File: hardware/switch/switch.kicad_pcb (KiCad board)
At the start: 2 copper layers, 70.5 x 70.5 mm, 27 parts, among them J1 Conn_01x07, J2 Conn_01x03, J3 Conn_01x05, J4 Conn_01x04, K1 G6SU-2, K2 G6SU-2, K3 G6SU-2, K4 G6SU-2, SW1 D2F-01, SW2 D2F-01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

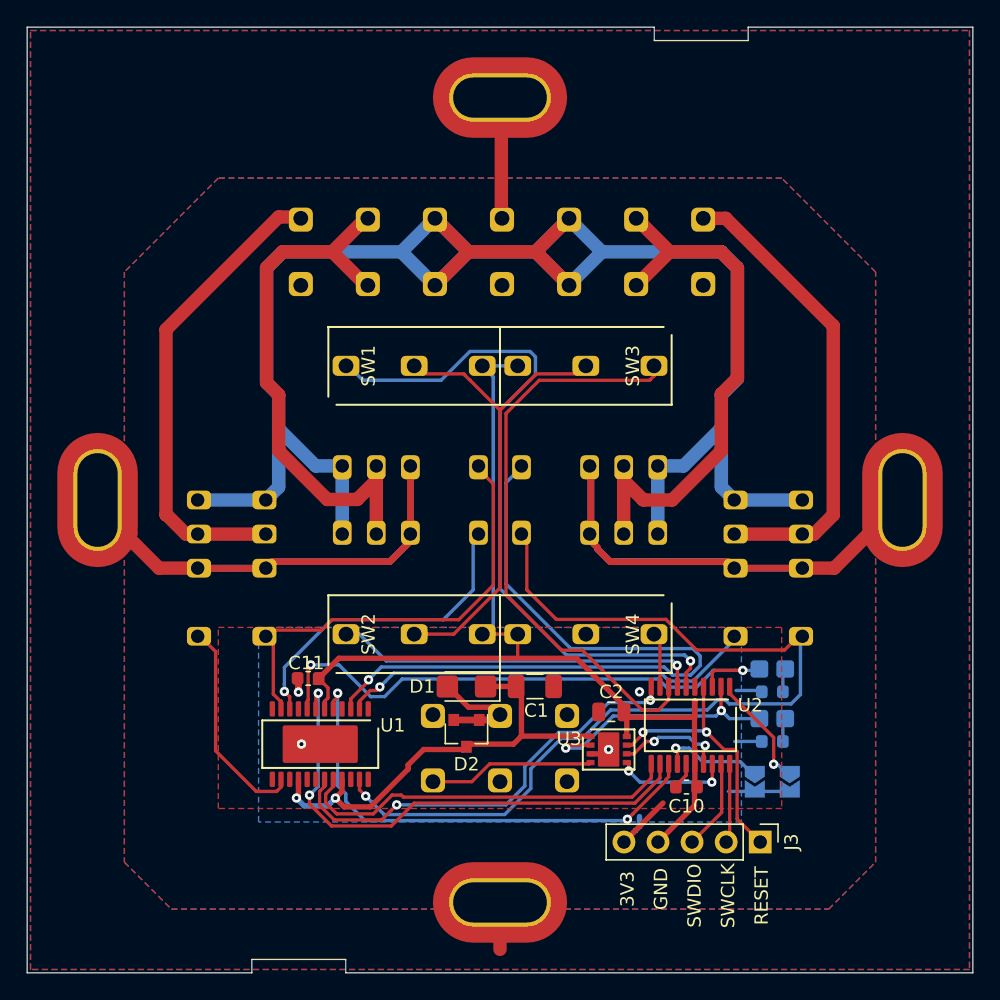
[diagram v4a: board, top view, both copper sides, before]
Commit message: Add indicator LEDs to switch
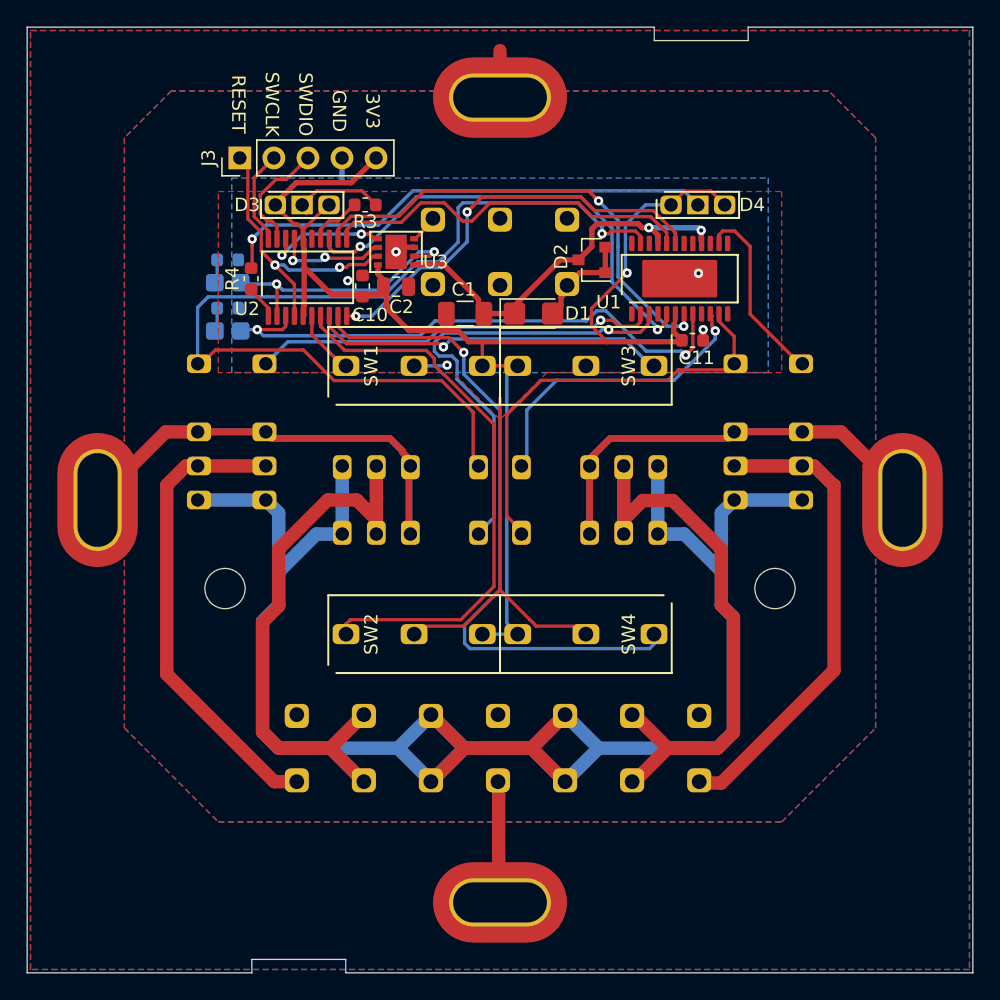
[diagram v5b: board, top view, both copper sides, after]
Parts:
- removed JP1, JP2: SolderJumper_2_Open, RoomControl:Jumper2
- added D5: LED, LED_SMD:LED_0805_2012Metric_Castellated, B.Cu at (79.7, 83.8)
- added D6: LED, LED_SMD:LED_0805_2012Metric_Castellated, B.Cu at (79.7, 87.4)
- added R3: 60R, Resistor_SMD:R_0603_1608Metric, F.Cu at (90.0, 78.0)
- added R4: 60R, Resistor_SMD:R_0603_1608Metric, F.Cu at (81.5, 83.5)
- D3, D4: value LED -> Conn_01x03; footprint LED_SMD:LED_0805_2012Metric_Castellated -> RoomControl:DiodeHoles3; moved to F.Cu
- moved J3 64.1 mm to (80.6, 74.5), turned to 90 degrees
- moved R1 54.2 mm to (79.7, 82.1), turned to 0 degrees
- moved D3 51.9 mm to (85.2, 78.0), turned to 0 degrees
- moved R2 49.7 mm to (79.7, 85.7), turned to 0 degrees
- moved J1 47.4 mm to (114.8, 118.5), turned to 90 degrees
- moved C10 44.5 mm to (89.8, 84.0), turned to 90 degrees
- moved U2 43.9 mm to (85.7, 83.4), turned to 90 degrees
- moved U1 43.8 mm to (113.4, 83.5), turned to 90 degrees
- moved U3 40.3 mm to (92.2, 81.5), turned to 180 degrees
- moved J2 38.3 mm to (105.0, 81.5), turned to 90 degrees
- moved C11 38.2 mm to (114.3, 88.1), turned to 0 degrees
- moved D2 36.5 mm to (106.8, 82.1), turned to 180 degrees
- moved C2 35.5 mm to (92.2, 84.1), turned to 0 degrees
- moved D4 35.0 mm to (114.8, 78.0), turned to 0 degrees
- moved C1 28.3 mm to (97.4, 86.1), turned to 180 degrees
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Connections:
- D3 pad 1: Net-(D3-Pad1) -> +3V3
- D3 pad 2: LIN_EN -> Net-(D3-Pad2)
- D4 pad 1: Net-(D4-Pad1) -> +3V3
- D4 pad 2: HB_EN -> Net-(D4-Pad2)
- J1 pad 1: KA1 -> KB1
- J1 pad 2: KA0 -> KB0
- J1 pad 6: KB0 -> KA0
- J1 pad 7: KB1 -> KA1
- J2 pad 1: LIN -> Net-(D1-Pad2)
- J2 pad 2: Net-(D1-Pad2) -> GND
- J2 pad 3: GND -> LIN
- J3 pad 4: +3V3 -> GND
- J3 pad 5: GND -> +3V3
- R1 pad 1: Net-(D3-Pad1) -> Net-(D5-Pad1)
- R2 pad 1: Net-(D4-Pad1) -> Net-(D6-Pad1)
- U1 pad 10: AX -> BX
- U1 pad 11: AY -> BY
- U1 pad 14: AZ -> BZ
- U1 pad 2: BZ -> AZ
- U1 pad 23: BY -> AY
- U1 pad 3: BX -> AX
- U2 pad 1: JPB -> LEDB
- U2 pad 14: JPA -> LEDA
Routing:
- net SWA0: track 52.4 -> 5.54 mm, vias 1 -> 0
- net SWB1: track 4.03 -> 50.0 mm, vias 0 -> 1
- net BY: track 70.8 -> 32.3 mm, vias 1 -> 0
- net Net-(D4-Pad2): track 0.00 -> 37.7 mm, vias 0 -> 1
- net AY: track 33.8 -> 70.8 mm, vias 0 -> 1
- net BX: track 55.1 -> 22.6 mm
- net +3V3: track 76.6 -> 104.7 mm, vias 0 -> 1
- net GND: track 56.1 -> 36.0 mm, vias 4 -> 5
- net BZ: track 31.2 -> 13.8 mm, vias 1 -> 0
- net SWB0: track 43.5 -> 26.7 mm, vias 0 -> 1
- net SWA1: track 27.2 -> 42.0 mm, vias 1 -> 0
- net AZ: track 16.0 -> 30.4 mm, vias 0 -> 1
- net AX: track 24.1 -> 34.9 mm
- net LIN: track 12.3 -> 2.15 mm
- net JPB: track 8.66 -> 0.00 mm, vias 1 -> 0
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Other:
- board text removed: "A"
- board text removed: "B"
